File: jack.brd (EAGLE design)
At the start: 44.2 x 26.4 mm, 35 parts, among them IC1 NUF2221W1T2G, IC2 ATSAMD21G18, IC3 LDO, J1 USB-micro, SW1 SPST3.5X6MM, X1 CX-3225 12.288MHz

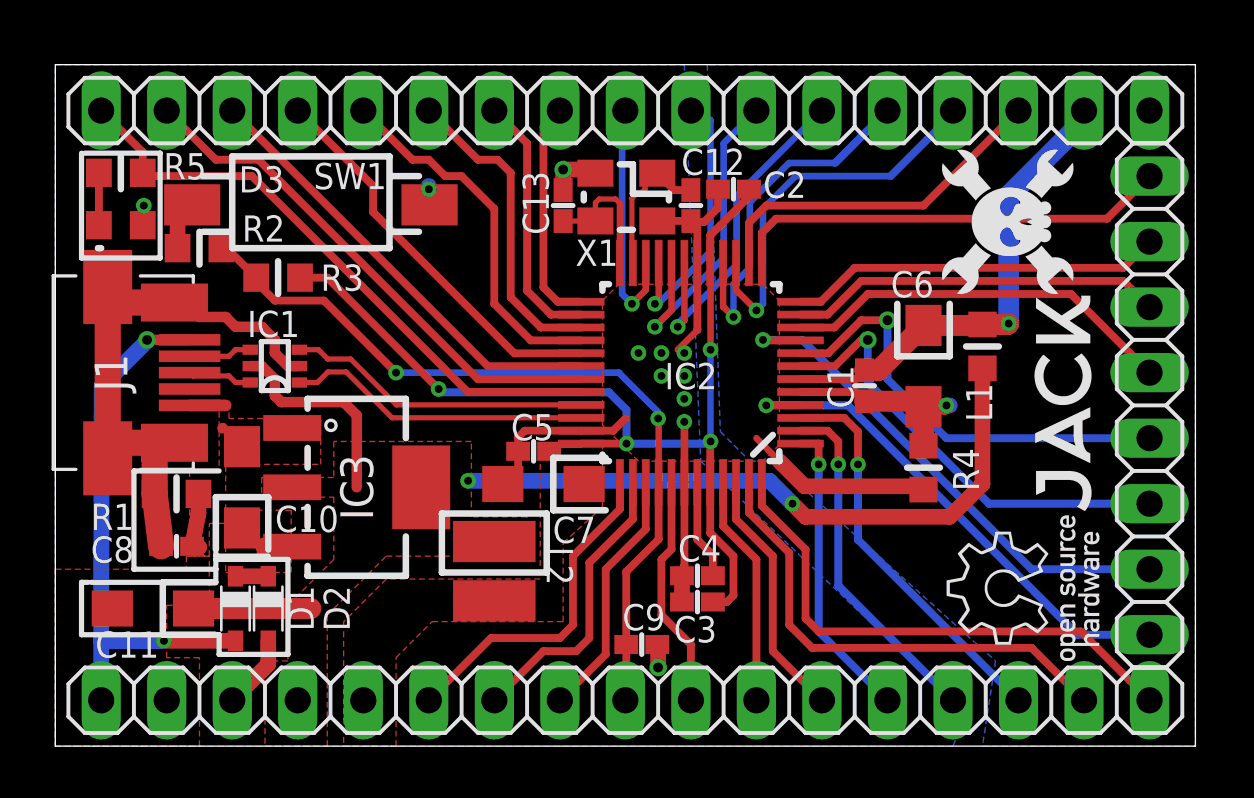
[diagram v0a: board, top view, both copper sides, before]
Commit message: Updated .sch and .brd to match changes in library files
Ops, I forgot to save and close the project before pushing the last
commit :grin:
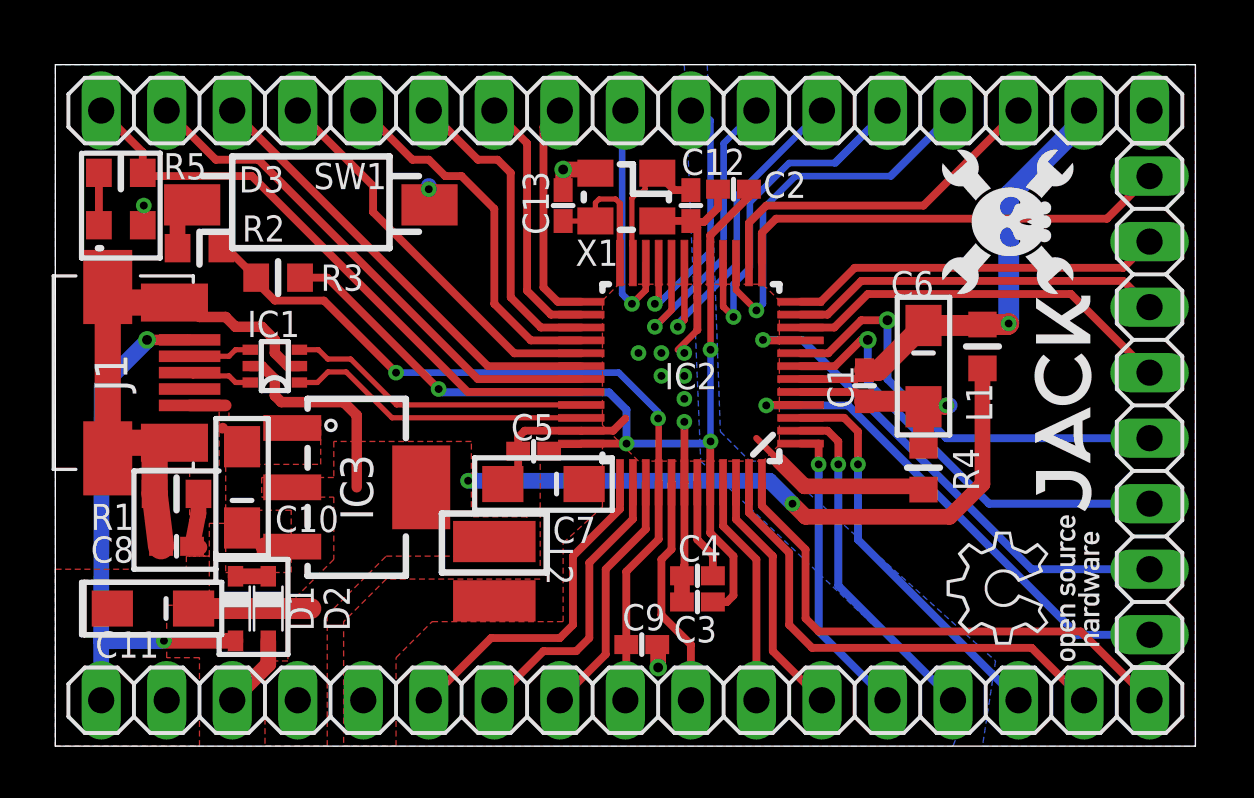
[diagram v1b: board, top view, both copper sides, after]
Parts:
- C1, C12, C13, C2, C3, C4, C5, C8, C9: device jack:C0402K -> jack:C0402
- C10, C11, C6, C7: device jack:SMC_P -> jack:CT3216
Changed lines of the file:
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@@
 <setting verticaltext="up"/>
 </settings>
-<grid distance="0.005" unitdist="inch" unit="inch" style="lines" multiple="1" display="no" altdistance="0.025" altunitdist="inch" altunit="inch"/>
+<grid distance="0.005" unitdist="inch" unit="mm" style="lines" multiple="1" display="no" altdistance="0.025" altunitdist="inch" altunit="inch"/>
 <layers>
 <layer number="1" name="Top" color="4" fill="1" visible="yes" active="yes"/>
@@
 <layer number="220" name="220bmp" color="7" fill="1" visible="no" active="yes"/>
 <layer number="221" name="221bmp" color="7" fill="1" visible="no" active="yes"/>
-<layer number="222" name="222bmp" color="7" fill="1" visible="no" active="yes"/>
 <layer number="223" name="223bmp" color="7" fill="1" visible="no" active="yes"/>
 <layer number="224" name="224bmp" color="7" fill="1" visible="no" active="yes"/>
@@
 </autorouter>
 <elements>
-<element name="C1" library="jack" package="C0402K" value="100nF" x="31.369" y="13.97" smashed="yes" rot="R270">
+<element name="C1" library="jack" package="C0402" value="100nF" x="31.369" y="13.97" smashed="yes" rot="R270">
 <attribute name="NAME" x="30.944" y="13.089" size="1.016" layer="25" rot="R90"/>
 <attribute name="VALUE" x="29.919" y="14.47" size="1.016" layer="27" rot="R270"/>
 </element>
-<element name="C10" library="jack" package="SMC_P" value="10uF" x="7.239" y="10.033" smashed="yes" rot="R90">
+<element name="C10" library="jack" package="CT3216" value="10uF" x="7.239" y="10.033" smashed="yes" rot="R90">
 <attribute name="NAME" x="8.517" y="8.299" size="1.016" layer="25"/>
 <attribute name="VALUE" x="8.689" y="9.533" size="1.016" layer="27" rot="R90"/>
 </element>
-<element name="C11" library="jack" package="SMC_P" value="10uF" x="3.7846" y="5.334" smashed="yes" rot="R180">
+<element name="C11" library="jack" package="CT3216" value="10uF" x="3.7846" y="5.334" smashed="yes" rot="R180">
 <attribute name="NAME" x="1.5494" y="3.429" size="1.016" layer="25"/>
 <attribute name="VALUE" x="4.4196" y="7.239" size="1.27" layer="27" rot="R180"/>
 </element>
-<element name="C12" library="jack" package="C0402K" value="15pF" x="24.638" y="20.955" smashed="yes" rot="R270">
+<element name="C12" library="jack" package="C0402" value="15pF" x="24.638" y="20.955" smashed="yes" rot="R270">
 <attribute name="NAME" x="24.265" y="22.142" size="1.016" layer="25"/>
 <attribute name="VALUE" x="23.188" y="21.455" size="1.016" layer="27" rot="R270"/>
 </element>
-<element name="C13" library="jack" package="C0402K" value="15pF" x="19.685" y="20.955" smashed="yes" rot="R90">
+<element name="C13" library="jack" package="C0402" value="15pF" x="19.685" y="20.955" smashed="yes" rot="R90">
 <attribute name="NAME" x="19.133" y="19.82" size="1.016" layer="25" rot="R90"/>
 <attribute name="VALUE" x="21.135" y="20.455" size="1.016" layer="27" rot="R90"/>
 </element>
-<element name="C2" library="jack" package="C0402K" value="100nF" x="26.289" y="21.59" smashed="yes" rot="R180">
+<element name="C2" library="jack" package="C0402" value="100nF" x="26.289" y="21.59" smashed="yes" rot="R180">
 <attribute name="NAME" x="27.44" y="21.253" size="1.016" layer="25"/>
 <attribute name="VALUE" x="26.789" y="23.04" size="1.016" layer="27" rot="R180"/>
 </element>
-<element name="C3" library="jack" package="C0402K" value="100nF" x="24.892" y="5.588" smashed="yes" rot="R180">
+<element name="C3" library="jack" package="C0402" value="100nF" x="24.892" y="5.588" smashed="yes" rot="R180">
 <attribute name="NAME" x="25.646" y="5.036" size="1.016" layer="25" rot="R180"/>
 <attribute name="VALUE" x="25.392" y="7.038" size="1.016" layer="27" rot="R180"/>
 </element>
-<element name="C4" library="jack" package="C0402K" value="100nF" x="24.892" y="6.604" smashed="yes" rot="R180">
+<element name="C4" library="jack" package="C0402" value="100nF" x="24.892" y="6.604" smashed="yes" rot="R180">
 <attribute name="NAME" x="24.138" y="7.156" size="1.016" layer="25"/>
 <attribute name="VALUE" x="25.392" y="8.054" size="1.016" layer="27" rot="R180"/>
 </element>
-<element name="C5" library="jack" package="C0402K" value="100nF" x="18.542" y="11.43" smashed="yes" rot="R180">
+<element name="C5" library="jack" package="C0402" value="100nF" x="18.542" y="11.43" smashed="yes" rot="R180">
 <attribute name="NAME" x="17.661" y="11.855" size="1.016" layer="25"/>
 <attribute name="VALUE" x="19.042" y="12.88" size="1.016" layer="27" rot="R180"/>
 </element>
-<element name="C6" library="jack" package="SMC_P" value="10uF" x="33.655" y="14.732" smashed="yes" rot="R270">
+<element name="C6" library="jack" package="CT3216" value="10uF" x="33.655" y="14.732" smashed="yes" rot="R270">
 <attribute name="NAME" x="32.385" y="17.399" size="1.016" layer="25"/>
 <attribute name="VALUE" x="31.75" y="15.367" size="1.27" layer="27" rot="R270"/>
 </element>
-<element name="C7" library="jack" package="SMC_P" value="10uF" x="18.923" y="10.16" smashed="yes" rot="R180">
+<element name="C7" library="jack" package="CT3216" value="10uF" x="18.923" y="10.16" smashed="yes" rot="R180">
 <attribute name="NAME" x="20.955" y="8.89" size="1.016" layer="25" rot="R180"/>
 <attribute name="VALUE" x="19.558" y="12.065" size="1.27" layer="27" rot="R180"/>
 </element>
-<element name="C8" library="jack" package="C0402K" value="4.5nF" x="4.699" y="7.747" smashed="yes">
+<element name="C8" library="jack" package="C0402" value="4.5nF" x="4.699" y="7.747" smashed="yes">
 <attribute name="NAME" x="3.048" y="8.128" size="1.016" layer="25" rot="R180"/>
 <attribute name="VALUE" x="4.064" y="5.842" size="1.27" layer="27"/>
 </element>
-<element name="C9" library="jack" package="C0402K" value="100nF" x="22.733" y="3.937" smashed="yes">
+<element name="C9" library="jack" package="C0402" value="100nF" x="22.733" y="3.937" smashed="yes">
 <attribute name="NAME" x="21.979" y="4.489" size="1.016" layer="25"/>
 <attribute name="VALUE" x="22.233" y="2.487" size="1.016" layer="27"/>

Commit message: :feelsgood: Added BOM, Gerbers, 3D model and render
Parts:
- R5: value 90 -> 68
- moved R3 0.13 mm to (8.76, 18.2)

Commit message: Update of gerber files
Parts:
- moved U$5 0.28 mm to (37.6, 20.4)
- moved C10 0.25 mm to (7.24, 10.3)
- moved C12 0.25 mm to (24.6, 21.2)
- moved C13 0.25 mm to (19.7, 21.2)
- moved C2 0.25 mm to (26.3, 21.8)
- moved C6 0.25 mm to (33.7, 15.0)
- moved IC1 0.25 mm to (8.51, 15.0)
- moved IC3 0.25 mm to (11.7, 10.3)
- moved R2 0.25 mm to (5.59, 19.6)
- moved X1 0.25 mm to (22.1, 21.5)
- moved C11 0.25 mm to (3.78, 5.59)
- moved D1 0.25 mm to (6.99, 5.59)
- moved D2 0.25 mm to (8.26, 5.59)
- moved L2 0.25 mm to (17.0, 6.99)
- moved C9 0.25 mm to (22.7, 4.19)
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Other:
- board size 44.2 x 26.4 mm -> 44.5 x 26.9 mm
- board text added: "Copyright © Michele Perla 2015 This documentation describes Open Hardware and is licensed under the CERN OHL v. 1.2. You may redistribute and modify this documentation under the terms of the CERN OHL v.1.2. (http://ohwr.org/cernohl). This documentation is distributed WITHOUT ANY EXPRESS OR IMPLIED WARRANTY, INCLUDING OF MERCHANTABILITY, SATISFACTORY QUALITY AND FITNESS FOR A PARTICULAR PURPOSE. P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"
